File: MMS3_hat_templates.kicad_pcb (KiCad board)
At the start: 4 copper layers, 100 x 50 mm, 55 parts, among them J1 Chainbus in, J2 Chainbus Out, J3 Conn_01x04_Pin, J4 AMASS XT60 Male, J5 AMASS XT60 Female, J8 Conn_01x03_Pin, SW1 SW_DIP_x04, U1 SN74CB3Q3384APW, U2 M24C64, U4 AMS1117, U5 LM2596HVS-ADJRG

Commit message: Updated footprints
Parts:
- removed C17, C19, C25, C26, C27, C28: 47u, Capacitor_SMD:CP_Elec_6.3x7.7
- removed C20, C21, C23, C24: 100nF, PCM_JLCPCB:C_0603
- removed C22: 3.3nF, PCM_JLCPCB:C_0603
- removed D1: LED, LED_SMD:LED_0603_1608Metric
- removed D2: MBRD10100CTTR, SMC_MBRD10100CTTR:TO-252-3_L6.5-W5.8-P4.58-TL
- removed J8: Conn_01x03_Pin, Connector_PinHeader_2.54mm:PinHeader_1x03_P2.54mm_Vertical
- removed L1: 100uH 4A, Inductor_SMD:L_Sunlord_SWRB1207S
- removed PN1: ~, PCM_JLCPCB:Part_Num_JLCPCB
- removed the R10 at (90.8, 129.0)
- removed R12: 1kΩ, PCM_JLCPCB:R_0402
- removed R13: 18.7k, PCM_JLCPCB:R_0402
- removed R14: 16.5k, PCM_JLCPCB:R_0402
- removed R15: 9.53k, PCM_JLCPCB:R_0402
- removed R16: 5.11k, PCM_JLCPCB:R_0402
- removed R17, R18: 33kΩ, PCM_JLCPCB:R_0402
- removed SW1: SW_DIP_x04, Button_Switch_THT:SW_DIP_SPSTx04_Slide_6.7x11.72mm_W7.62mm_P2.54mm_LowProfile
- removed TP8: TestPoint, TestPoint:TestPoint_Pad_D1.0mm
- removed U5: LM2596HVS-ADJRG, Package_TO_SOT_SMD:TO-263-5_TabPin3
- added D3: Red, PCM_JLCPCB:D_0603, F.Cu at (176.3, 97.7)
- added R2: 10kΩ, PCM_JLCPCB:R_0402, F.Cu at (138.0, 111.2)
- added R3: 10kΩ, PCM_JLCPCB:R_0402, F.Cu at (139.8, 111.2)
- added R5: 10kΩ, PCM_JLCPCB:R_0402, F.Cu at (141.7, 111.2)
- added R7: 10kΩ, PCM_JLCPCB:R_0402, F.Cu at (143.6, 111.2)
- added R8: 10kΩ, PCM_JLCPCB:R_0402, F.Cu at (145.4, 111.2)
- added R9: 10kΩ, PCM_JLCPCB:R_0402, F.Cu at (147.2, 111.2)
- D4: value MBRD10100CTTR -> SS510C; footprint SMC_MBRD10100CTTR:TO-252-3_L6.5-W5.8-P4.58-TL -> SS510C:SMC_L7.1-W6.2-LS8.1-RD
- R11: value 33kΩ -> 10kΩ
- moved H9 103.4 mm to (177.0, 137.0)
- moved R11 61.8 mm to (149.1, 111.2), turned to 90 degrees
- moved H7 47.5 mm to (79.0, 89.5)
- moved D4 29.4 mm to (92.5, 94.7)
- moved R6 18.9 mm to (152.0, 107.0), turned to 0 degrees
- moved J5 17.9 mm to (89.2, 119.2)
- moved J4 16.0 mm to (90.2, 109.8)
- moved R10 13.6 mm to (152.0, 109.5), turned to 0 degrees
- moved C18 10.6 mm to (166.7, 96.9), turned to 0 degrees
- moved H8 7.35 mm to (177.0, 89.5)
- moved U2 3.49 mm to (168.6, 103.6)
- moved U4 3.30 mm to (160.8, 96.9)
- moved C2 2.36 mm to (171.9, 105.4), turned to 90 degrees
- moved C16 2.32 mm to (166.6, 94.6), turned to 0 degrees
- moved J3 1.99 mm to (175.9, 108.2)
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- renumbered R3 to R10, R2 to R6
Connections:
- D4 pad 1: GND -> BRD_VIN
- D4 pad 2: Net-(D4-K) -> Vin
- R11 pad 1: Net-(C20-Pad2) -> /Bus_switch/Chainbus.MOSI
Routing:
- net Vin: track 64.3 -> 4.03 mm
- net U_reg: track 55.0 -> 0.00 mm, vias 2 -> 0
- net Net-(U5-FB): track 38.3 -> 0.00 mm, vias 1 -> 0
- net /Bus_switch/Chainbus.SDA: track 14.5 -> 38.9 mm, vias 0 -> 2
- net Net-(D4-K): track 21.4 -> 0.00 mm
- net /Bus_switch/Chainbus.SCL: track 15.5 -> 35.6 mm
- net Net-(R14-Pad1): track 13.8 -> 0.00 mm, vias 1 -> 0
- net Net-(R15-Pad1): track 8.34 -> 0.00 mm
- net GND: track 21.6 -> 17.9 mm, vias 142 -> 25
- net Net-(R16-Pad1): track 3.06 -> 0.00 mm
- net +5V: track 59.4 -> 58.0 mm, vias 5 -> 3
- net +3V3: track 57.0 -> 55.9 mm, vias 3 -> 4
- net Net-(D3-Pad2): track 2.38 -> 1.57 mm
- net /Bus_switch/Chainbus.CS: track 0.00 -> 0.76 mm
- net /Bus_switch/SEL1: track 82.3 -> 82.9 mm, vias 6 -> 4
- removed copper zone on In1.Cu, net GND
- removed copper zone on In2.Cu, net GND
- removed copper zone on F.Cu, net Net-(C20-Pad2)
- removed copper zone on F.Cu, net Net-(C23-Pad2)
- removed copper zone on F.Cu, net Net-(D4-K)
- removed copper zone on F.Cu, net Net-(J8-Pin_1)
- removed copper zone on F.Cu, net U_reg
- removed copper zone on B.Cu, net Vin
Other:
- copper layers 4 -> 2
- board text added: "Front and Back keepout zone for DIN rail mount"
- board text added: "J1"
- board text added: "J2"
- board text added: "SN74CB3Q3384APW"
- board text added: "TMC5130A-TA"
- board text added: "U1"
- board text removed: "DONT change SW1 WITH POWER ON"
- board text removed: "SW1 24 9 12 6.2"

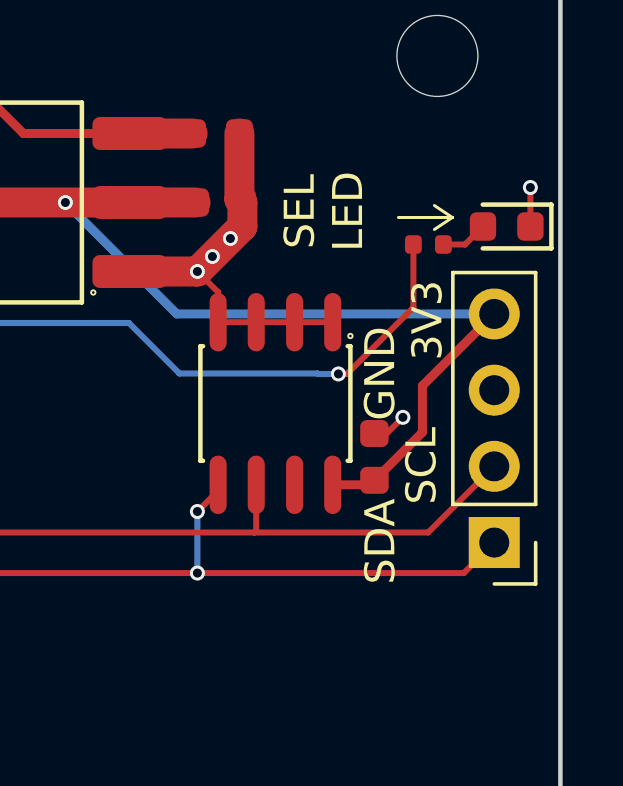
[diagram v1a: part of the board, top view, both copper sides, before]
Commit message: fixed selected led polarity
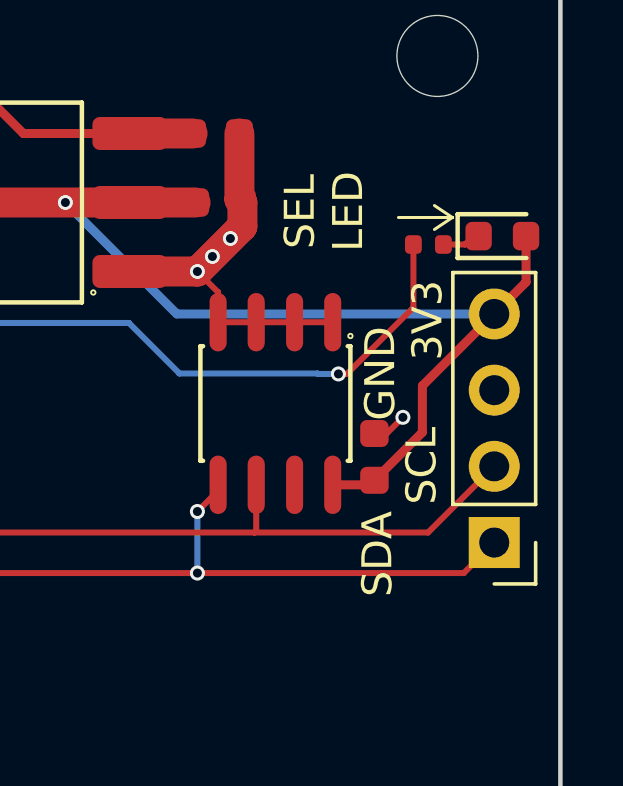
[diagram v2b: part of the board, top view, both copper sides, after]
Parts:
- moved D3 0.35 mm to (176.2, 98.0), turned to 0 degrees
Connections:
- D3 pad 1: GND -> Net-(D3-Pad1)
- D3 pad 2: Net-(D3-Pad2) -> +3V3
- R1 pad 2: Net-(D3-Pad2) -> Net-(D3-Pad1)
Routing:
- net +3V3: track 55.9 -> 59.0 mm
- net Net-(D3-Pad2): track 1.57 -> 0.00 mm
- net Net-(D3-Pad1): track 0.00 -> 1.57 mm
- net GND: track 17.9 -> 16.6 mm, vias 25 -> 24

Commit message: minor aesthetic changes
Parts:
- moved J5 19.6 mm to (106.9, 127.5), turned to 180 degrees
- moved J4 18.2 mm to (97.5, 126.5), turned to 180 degrees
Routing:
- net Vin: track 4.03 -> 32.6 mm

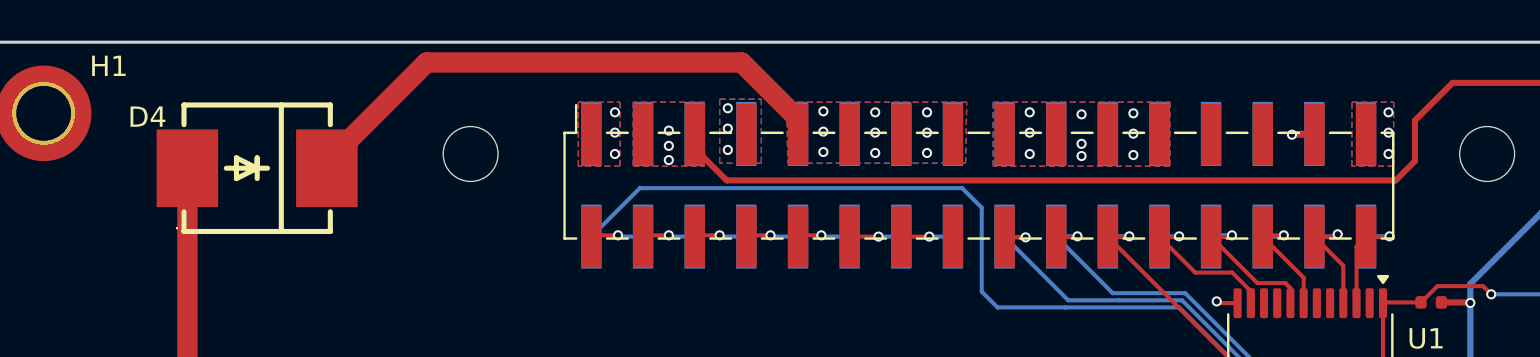
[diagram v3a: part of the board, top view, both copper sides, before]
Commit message: fixed 50V clearance net class
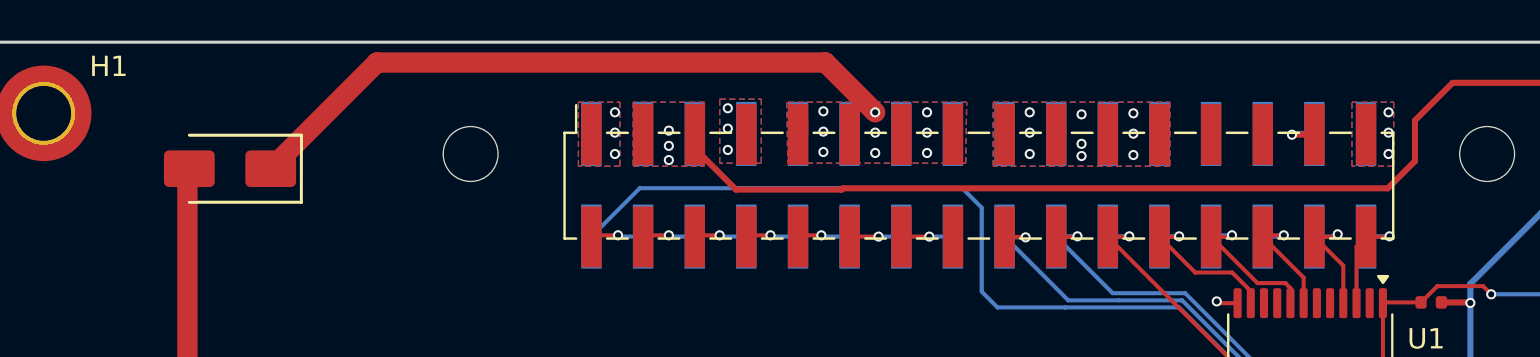
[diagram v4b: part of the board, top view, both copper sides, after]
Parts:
- removed D4: SS510C, SS510C:SMC_L7.1-W6.2-LS8.1-RD
- added D1: M7, PCM_JLCPCB:D_SMA, F.Cu at (91.2, 94.7)
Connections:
- net BRD_VIN renamed VIN_CHAINBUS
- net Vin renamed /Power Connector/VIN_BRD
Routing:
- net VIN_CHAINBUS: track 27.1 -> 33.7 mm
